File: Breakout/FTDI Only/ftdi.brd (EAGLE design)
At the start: 19.4 x 22.8 mm, 28 parts, among them Q1 16Mhz, U5 93LC46BT-I/OT

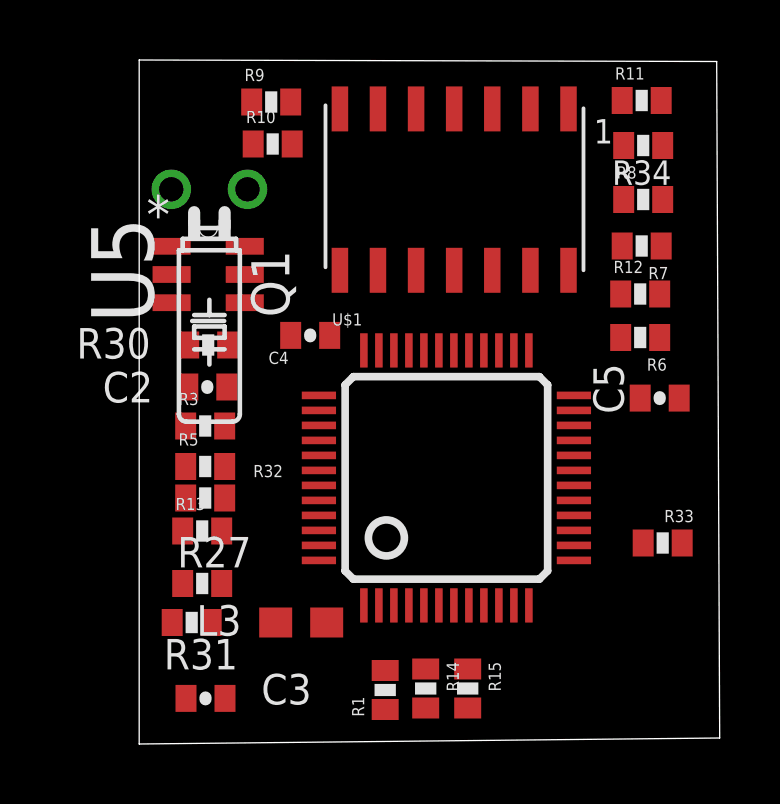
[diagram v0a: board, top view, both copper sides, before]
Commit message: replace chip
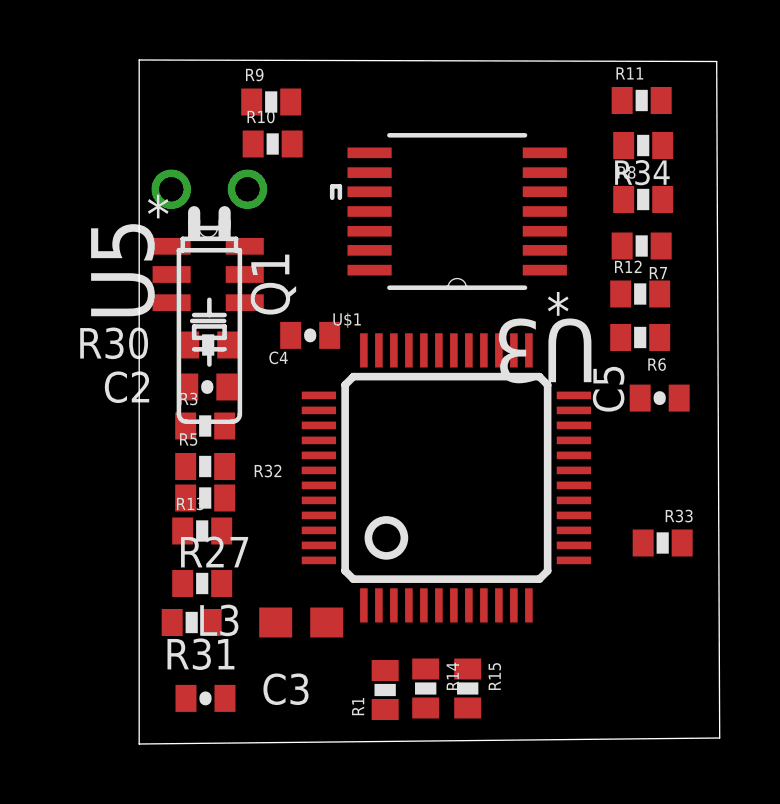
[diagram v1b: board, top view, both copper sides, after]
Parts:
- removed U$3: DECADE-74LVC125A, DECADE-libraries:DECADE-SO-14
- added U3: SN74LVC125APWR, Texas Instruments_By_element14_Batch_1:SOP65P640X120-14N
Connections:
- net DBGEN_N: now also U3.1; no longer U$3.1
- net DBG_RST_N: now also U3.4; no longer U$3.4
- net FT_SK: now also U3.2; no longer U$3.2
- net GND: now also U3.7; no longer U$3.7
- net N$49: now also U3.5; no longer U$3.5
- net N$50: now also U3.6; no longer U$3.6
- net TCK: now also U3.3; no longer U$3.3
- net VCC: now also U3.14; no longer U$3.14
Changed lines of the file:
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@@
 <attribute name="VALUE" x="16.6205" y="12.477" size="0.4064" layer="27"/>
 </element>
-<element name="U$3" library="DECADE-libraries" package="DECADE-SO-14" value="DECADE-74LVC125A" x="22.71" y="18.29" rot="R180"/>
 <element name="C5" library="SparkFun-Passives" package="0402-CAP" value="0.1uF" x="29.35" y="11.53" smashed="yes" rot="R180">
 <attribute name="NAME" x="27.139" y="12.6815" size="1.016" layer="25" font="vector" ratio="20" rot="R270"/>
@@
 <element name="R1" library="SparkFun-Passives" package="0402-RES" value="28" x="20.2" y="1.8" rot="R90"/>
 <element name="R15" library="SparkFun-Passives" package="0402-RES" value="28" x="22.95" y="1.85" rot="R270"/>
+<element name="U3" library="Texas Instruments_By_element14_Batch_1" package="SOP65P640X120-14N" value="SN74LVC125APWR" x="22.6" y="17.75" rot="R180">
+<attribute name="PACKAGE" value="TSSOP14" x="22.6" y="17.75" size="1.778" layer="27" rot="R180" display="off"/>
+<attribute name="OC_NEWARK" value="35K0816" x="22.6" y="17.75" size="1.778" layer="27" rot="R180" display="off"/>
+<attribute name="MPN" value="SN74LVC125APWR" x="22.6" y="17.75" size="1.778" layer="27" rot="R180" display="off"/>
+<attribute name="SUPPLIER" value="TEXAS INSTRUMENTS" x="22.6" y="17.75" size="1.778" layer="27" rot="R180" display="off"/>
+<attribute name="OC_FARNELL" value="1102981" x="22.6" y="17.75" size="1.778" layer="27" rot="R180" display="off"/>
+</element>
 </elements>
 <signals>
@@
 <contactref element="U$1" pad="47"/>
 <contactref element="C4" pad="1"/>
-<contactref element="U$3" pad="7"/>
 <contactref element="C5" pad="1"/>
 <contactref element="U5" pad="2"/>
 <contactref element="R10" pad="2"/>
-<wire x1="14.92" y1="11.9" x2="17.1" y2="20" width="0" layer="19" extent="1-1"/>
-<wire x1="17.05" y1="13.62" x2="14.92" y2="11.9" width="0" layer="19" extent="1-1"/>
-<wire x1="13.0808" y1="15.65" x2="14.92" y2="11.9" width="0" layer="19" extent="1-1"/>
-<wire x1="13.56" y1="1.52" x2="13.0808" y2="15.65" width="0" layer="19" extent="1-1"/>
-<wire x1="17.99" y1="7.62" x2="13.56" y2="1.52" width="0" layer="19" extent="1-1"/>
-<wire x1="17.99" y1="6.62" x2="17.99" y2="7.62" width="0" layer="19" extent="1-1"/>
-<wire x1="23.49" y1="4.62" x2="17.99" y2="6.62" width="0" layer="19" extent="1-1"/>
-<wire x1="26.49" y1="8.62" x2="23.49" y2="4.62" width="0" layer="19" extent="1-1"/>
-<wire x1="30" y1="11.53" x2="26.49" y2="8.62" width="0" layer="19" extent="1-1"/>
+<contactref element="U3" pad="7"/>
+<wire x1="26.49" y1="8.62" x2="30" y2="11.53" width="0" layer="19" extent="1-1"/>
 <wire x1="24.99" y1="13.12" x2="26.49" y2="8.62" width="0" layer="19" extent="1-1"/>
 <wire x1="20.49" y1="13.12" x2="24.99" y2="13.12" width="0" layer="19" extent="1-1"/>
-<wire x1="18.69" y1="21.17" x2="24.99" y2="13.12" width="0" layer="19" extent="1-1"/>
+<wire x1="25.521" y1="19.7058" x2="20.49" y2="13.12" width="0" layer="19" extent="1-1"/>
+<wire x1="17.05" y1="13.62" x2="25.521" y2="19.7058" width="0" layer="19" extent="1-1"/>
+<wire x1="14.92" y1="11.9" x2="17.05" y2="13.62" width="0" layer="19" extent="1-1"/>
+<wire x1="13.0808" y1="15.65" x2="14.92" y2="11.9" width="0" layer="19" extent="1-1"/>
+<wire x1="17.1" y1="20" x2="25.521" y2="19.7058" width="0" layer="19" extent="1-1"/>
+<wire x1="23.49" y1="4.62" x2="26.49" y2="8.62" width="0" layer="19" extent="1-1"/>
+<wire x1="17.99" y1="7.62" x2="14.92" y2="11.9" width="0" layer="19" extent="1-1"/>
+<wire x1="17.99" y1="6.62" x2="17.99" y2="7.62" width="0" layer="19" extent="1-1"/>
+<wire x1="13.56" y1="1.52" x2="17.99" y2="6.62" width="0" layer="19" extent="1-1"/>
 </signal>
 <signal name="VCC">
-<contactref element="U$3" pad="14"/>
 <contactref element="U$1" pad="31"/>
 <contactref element="U$1" pad="14"/>
@@
 <contactref element="R33" pad="1"/>
 <contactref element="R12" pad="1"/>
-<wire x1="13.1" y1="4.05" x2="28.05" y2="15" width="0" layer="19" extent="1-1"/>
-<wire x1="13.45" y1="5.35" x2="13.1" y2="4.05" width="0" layer="19" extent="1-1"/>
-<wire x1="14.95" y1="13.3" x2="13.45" y2="5.35" width="0" layer="19" extent="1-1"/>
-<wire x1="15.5192" y1="16.5898" x2="13.45" y2="5.35" width="0" layer="19" extent="1-1"/>
-<wire x1="21.99" y1="13.12" x2="15.5192" y2="16.5898" width="0" layer="19" extent="1-1"/>
+<contactref element="U3" pad="14"/>
+<wire x1="28.05" y1="15" x2="19.679" y2="15.7942" width="0" layer="19" extent="1-1"/>
+<wire x1="21.99" y1="13.12" x2="28.05" y2="15" width="0" layer="19" extent="1-1"/>
+<wire x1="14.95" y1="13.3" x2="21.99" y2="13.12" width="0" layer="19" extent="1-1"/>
+<wire x1="15.5192" y1="16.5898" x2="14.95" y2="13.3" width="0" layer="19" extent="1-1"/>
 <wire x1="26.49" y1="6.62" x2="21.99" y2="13.12" width="0" layer="19" extent="1-1"/>
 <wire x1="30.1" y1="6.7" x2="26.49" y2="6.62" width="0" layer="19" extent="1-1"/>
-<wire x1="26.31" y1="15.79" x2="21.99" y2="13.12" width="0" layer="19" extent="1-1"/>
+<wire x1="13.45" y1="5.35" x2="14.95" y2="13.3" width="0" layer="19" extent="1-1"/>
+<wire x1="13.1" y1="4.05" x2="13.45" y2="5.35" width="0" layer="19" extent="1-1"/>
 </signal>
 <signal name="+5V_USB">
@@
 </signal>
 <signal name="TCK">
-<contactref element="U$3" pad="3"/>
 <contactref element="R11" pad="1"/>
-<wire x1="23.77" y1="21.17" x2="28.1" y2="21.45" width="0" layer="19" extent="1-1"/>
+<contactref element="U3" pad="3"/>
+<wire x1="25.521" y1="17.0896" x2="28.1" y2="21.45" width="0" layer="19" extent="1-1"/>
 </signal>
 <signal name="DBGEN_N">
-<contactref element="U$3" pad="1"/>
 <contactref element="R6" pad="1"/>
-<wire x1="26.31" y1="21.17" x2="29.35" y2="13.55" width="0" layer="19" extent="1-1"/>
+<contactref element="U3" pad="1"/>
+<wire x1="25.521" y1="15.7942" x2="29.35" y2="13.55" width="0" layer="19" extent="1-1"/>
 </signal>
 <signal name="FT_SK">
-<contactref element="U$3" pad="2"/>
 <contactref element="R8" pad="1"/>
-<wire x1="25.04" y1="21.17" x2="28.15" y2="18.15" width="0" layer="19" extent="1-1"/>
+<contactref element="U3" pad="2"/>
+<wire x1="25.521" y1="16.4546" x2="28.15" y2="18.15" width="0" layer="19" extent="1-1"/>
 </signal>
 <signal name="N$46">
@@
 </signal>
 <signal name="DBG_RST_N">
-<contactref element="U$3" pad="4"/>
 <contactref element="R7" pad="1"/>
 <contactref element="R12" pad="2"/>
-<wire x1="29.4" y1="16.6" x2="29.35" y2="15" width="0" layer="19" extent="1-1"/>
-<wire x1="22.5" y1="21.17" x2="29.4" y2="16.6" width="0" layer="19" extent="1-1"/>
+<contactref element="U3" pad="4"/>
+<wire x1="29.35" y1="15" x2="29.4" y2="16.6" width="0" layer="19" extent="1-1"/>
+<wire x1="25.521" y1="17.75" x2="29.4" y2="16.6" width="0" layer="19" extent="1-1"/>
 </signal>
 <signal name="N$49">
-<contactref element="U$3" pad="5"/>
 <contactref element="R10" pad="1"/>
-<wire x1="21.23" y1="21.17" x2="15.8" y2="20" width="0" layer="19" extent="1-1"/>
+<contactref element="U3" pad="5"/>
+<wire x1="25.521" y1="18.4104" x2="15.8" y2="20" width="0" layer="19" extent="1-1"/>
 </signal>
 <signal name="N$50">
-<contactref element="U$3" pad="6"/>
 <contactref element="R9" pad="1"/>
-<wire x1="19.96" y1="21.17" x2="15.75" y2="21.4" width="0" layer="19" extent="1-1"/>
+<contactref element="U3" pad="6"/>
+<wire x1="25.521" y1="19.0454" x2="15.75" y2="21.4" width="0" layer="19" extent="1-1"/>
 </signal>
 <signal name="N$51">
